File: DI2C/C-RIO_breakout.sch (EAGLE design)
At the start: 36 parts, among them X1 GLX-S-88M, X2 GLX-S-88M, X3 GLX-S-88M, X4 GLX-S-88M

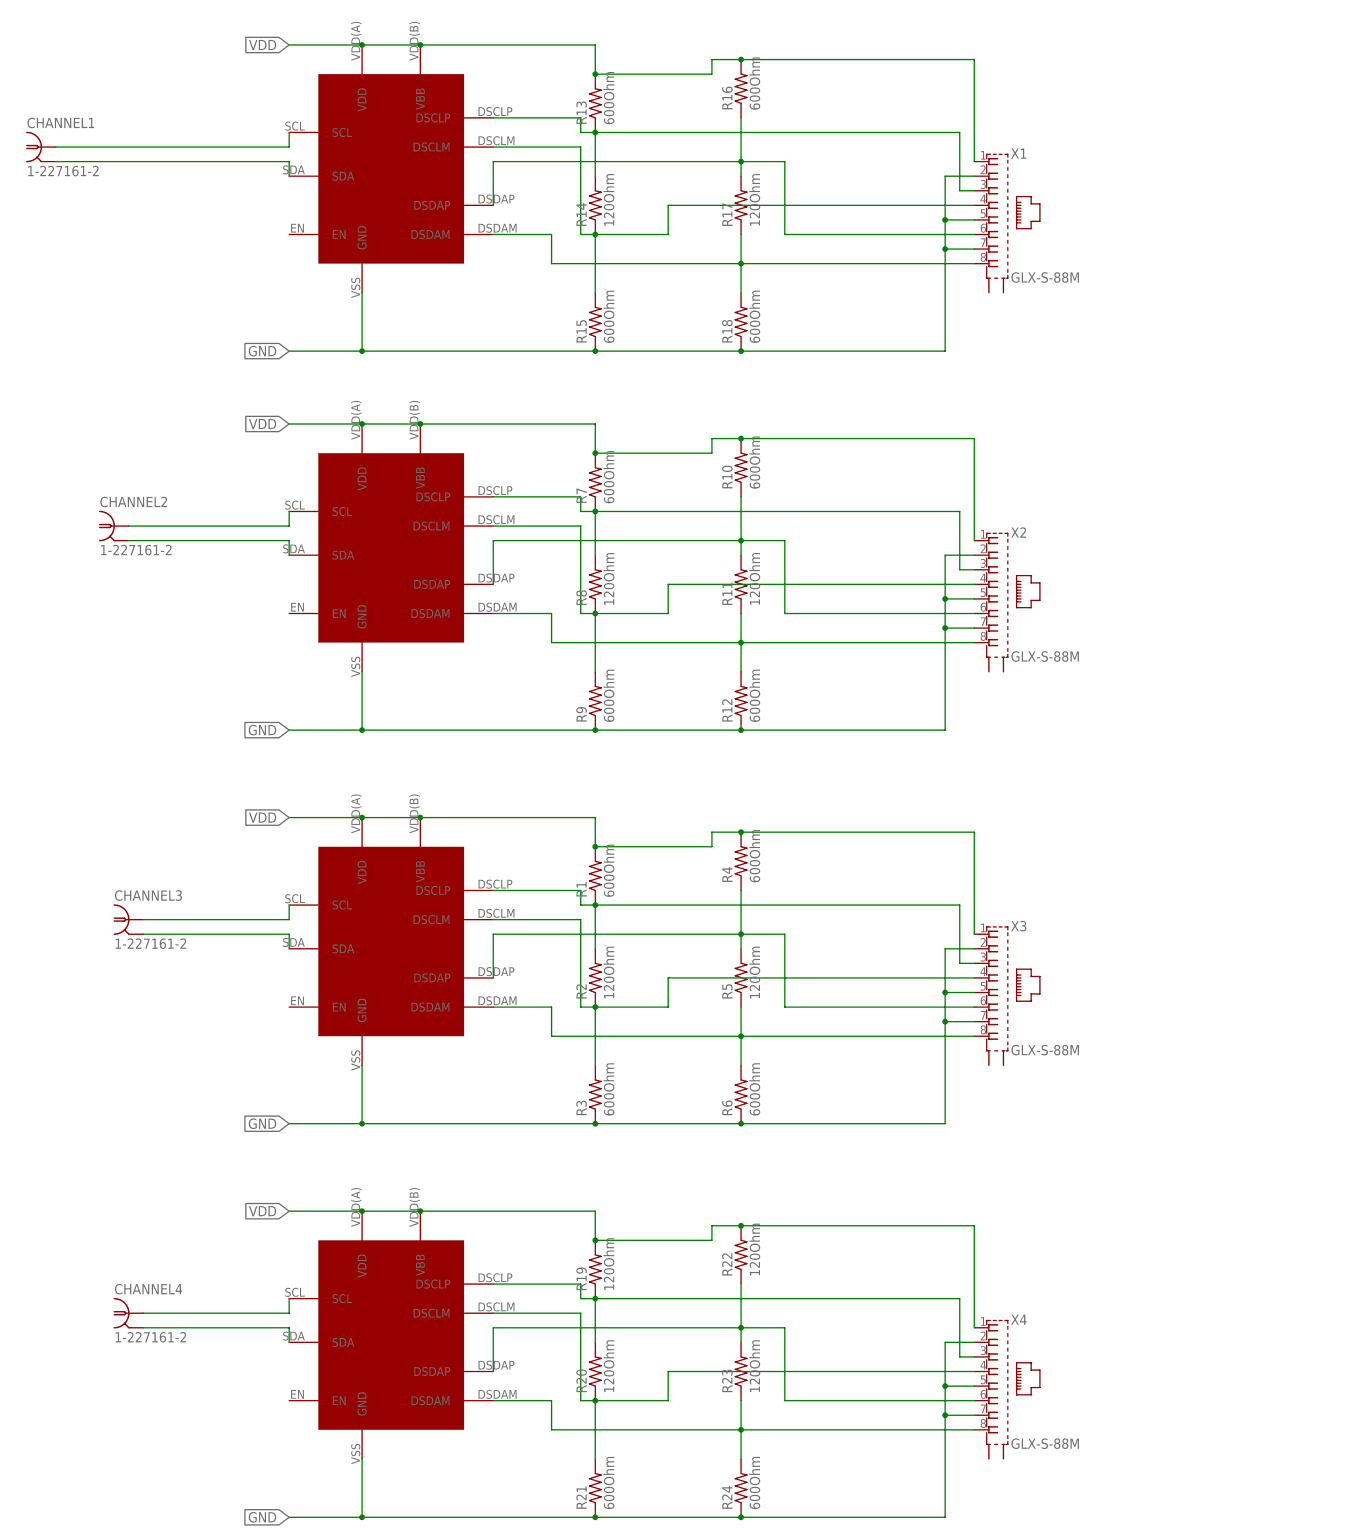
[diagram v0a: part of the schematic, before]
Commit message: finish i2c base master board
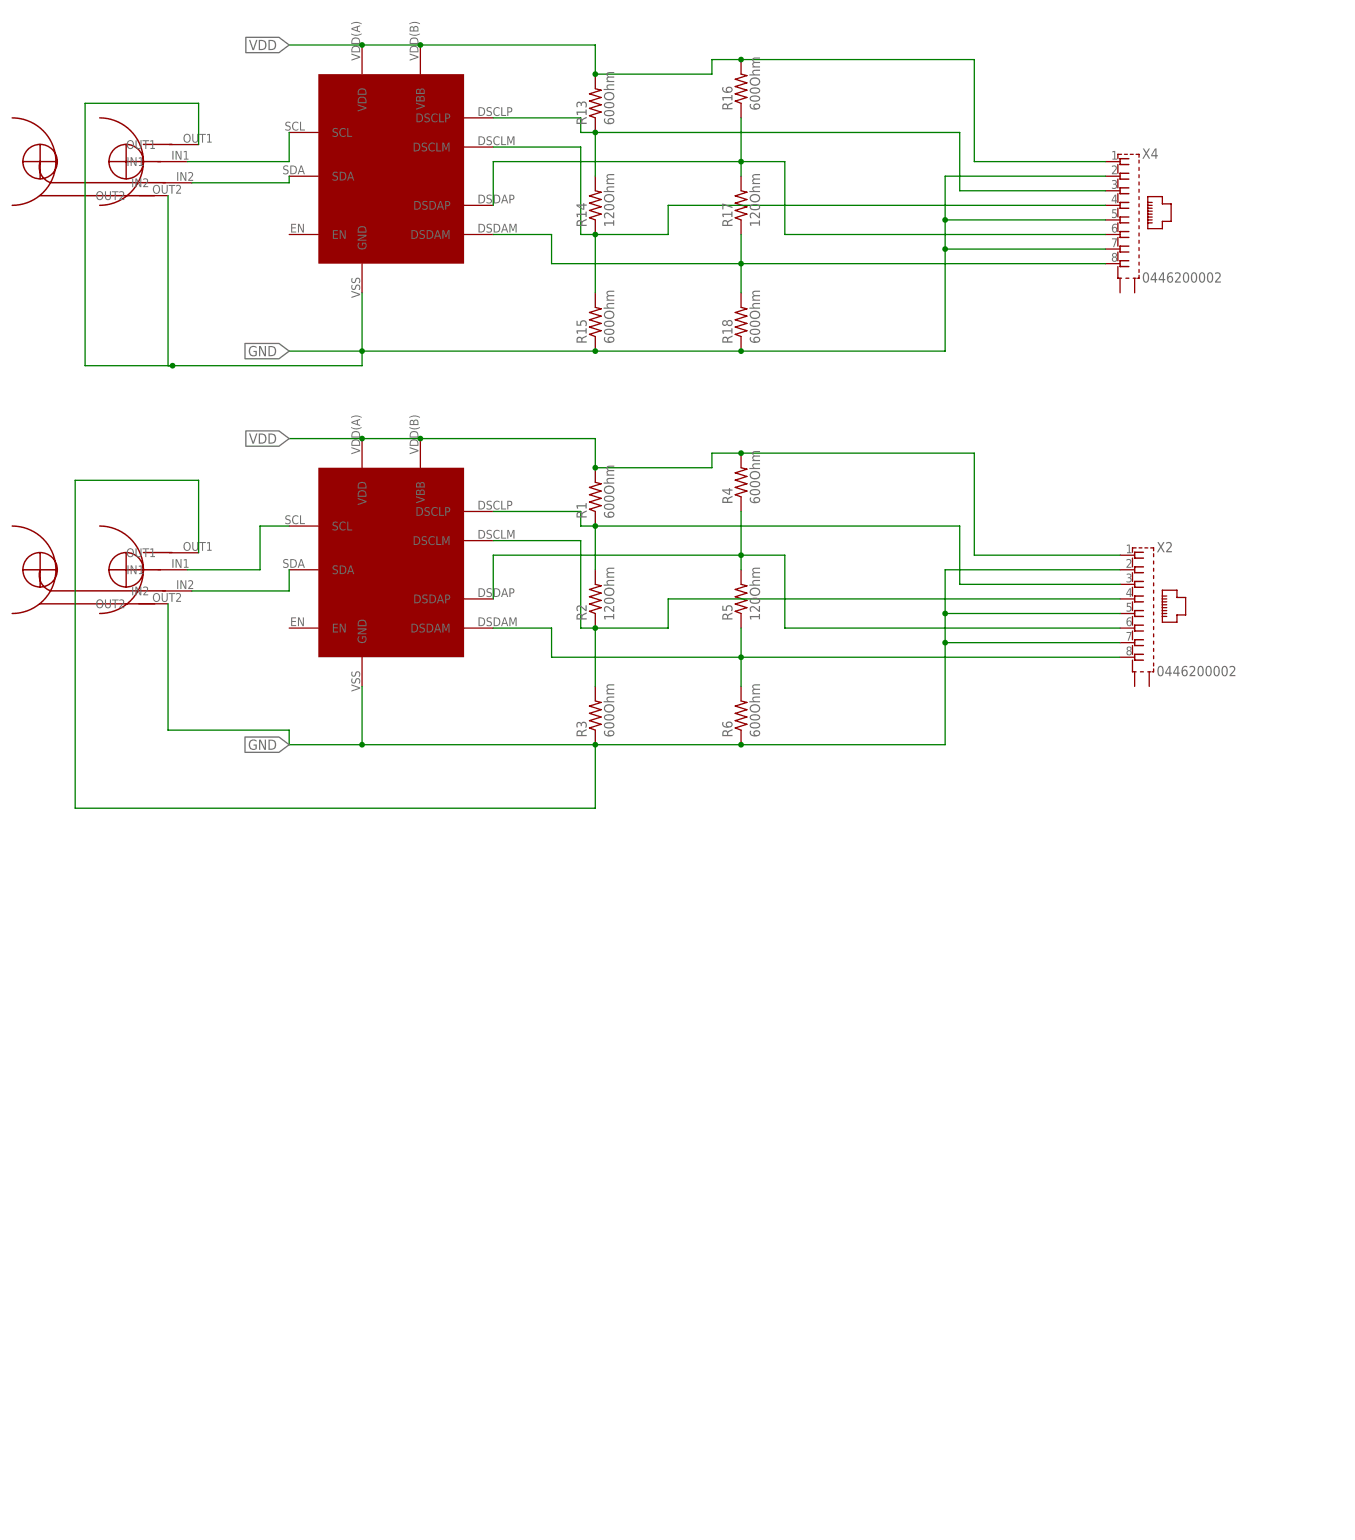
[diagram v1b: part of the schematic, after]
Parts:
- removed CHANNEL1, CHANNEL2, CHANNEL3, CHANNEL4: 1-227161-2, con-coax:1-227161-2
- removed R10, R12, R21, R24, R7, R9: 600Ohm, resistor:R-US_0414/15
- removed R11, R19, R20, R22, R23, R8: 120Ohm, resistor:R-US_0414/15
- removed X1, X3: GLX-S-88M, con-kycon:GLX-S-88M
- U$2, U$4: value PCA9615 -> DUALBNC_CONNECTOR; device PCA9615:PCA9615 -> PCA9615:DUALBNC_CONNECTOR
- X2, X4: value GLX-S-88M -> 0446200002; device con-kycon:GLX-S-88M -> con-molex:0446200002
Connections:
- removed net N$10: R11.1, R12.2, U$2.DSDAM, X2.8
- removed net N$13: R22.1, R23.2, U$4.DSDAP, X4.6
- removed net N$14: R23.1, R24.2, U$4.DSDAM, X4.8
- removed net N$17: CHANNEL4.1, U$4.SCL
- removed net N$18: CHANNEL4.2, U$4.SDA
- removed net N$19: CHANNEL3.2, U$1.SDA
- removed net N$20: CHANNEL3.1, U$1.SCL
- removed net N$21: CHANNEL2.2, U$2.SDA
- removed net N$22: CHANNEL2.1, U$2.SCL
- removed net N$23: CHANNEL1.2, U$3.SDA
- removed net N$24: CHANNEL1.1, U$3.SCL
- removed net N$9: R10.1, R11.2, U$2.DSDAP, X2.6
- net GND: now also U$2.OUT1, U$2.OUT2, U$4.OUT1, U$4.OUT2; no longer R12.1, R21.1, R24.1, R9.1, U$2.GND, U$4.GND, X1.2, X1.5, X1.7, X3.2, X3.5, X3.7
- net N$1: now also X2.3; no longer X3.3
- net N$11: now also X4.3; no longer X1.3
- net N$12: now also X4.4; no longer X1.4
- net N$15: now also X4.6; no longer X1.6
- net N$16: now also X4.8; no longer X1.8
- net N$2: now also U$1.SCL, U$4.IN1; no longer R19.1, R20.2, U$4.DSCLP, X4.3
- net N$3: now also X2.4; no longer X3.4
- net N$4: now also X2.6; no longer X3.6
- net N$5: now also X2.8; no longer X3.8
- net N$6: now also U$1.SDA, U$4.IN2; no longer R7.1, R8.2, U$2.DSCLP, X2.3
- net N$7: now also U$2.IN1, U$3.SCL; no longer R20.1, R21.2, U$4.DSCLM, X4.4
- net N$8: now also U$2.IN2, U$3.SDA; no longer R8.1, R9.2, U$2.DSCLM, X2.4
- net VDD: no longer R10.2, R19.2, R22.2, R7.2, U$2.VBB, U$2.VDD, U$4.VBB, U$4.VDD, X1.1, X3.1
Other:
- moved on the sheet: R1, R2, R3, R4, R5, R6

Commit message: update schmeatic
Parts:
- removed X2, X4: 0446200002, con-molex:0446200002
- added R10, R7, R8, R9: 600Ohm, resistor:R-US_0414/15
- added T1, T2, T3, T4: 2N2222, transistor-neu-to92:2N2222
- added TOF1, TOF2, TOF3, TOF4, U$6: RJ45-8N4-B, con-amphenol-rj45-ld:RJ45-8N4-B
- added X1: (no value), con-subd:F37HPS
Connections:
- net N$2 renamed SCL1
- net N$6 renamed SDA1
- net N$7 renamed SCL2
- net N$8 renamed SDA2
- removed net N$1: R1.1, R2.2, U$1.DSCLP, X2.3
- removed net N$3: R2.1, R3.2, U$1.DSCLM, X2.4
- removed net N$5: R5.1, R6.2, U$1.DSDAM, X2.8
- new net DSCLM1: R2.1, R3.2, TOF1.NC1, TOF2.NC1, TOF3.NC1, TOF4.NC1, U$1.DSCLM
- new net DSCLP1: R1.1, R2.2, TOF1.TX-, TOF2.TX-, TOF3.TX-, TOF4.TX-, U$1.DSCLP
- new net DSDAM1: R5.1, R6.2, TOF1.TX0, TOF2.TX0, TOF3.TX0, TOF4.TX0, U$1.DSDAM
- new net DSDAP1: TOF1.RX0, TOF2.RX0, TOF3.RX0, TOF4.RX0
- new net GND2: TOF1.GND1, TOF1.GND2, TOF2.GND1, TOF2.GND2, TOF3.GND1, TOF3.GND2, TOF4.GND1, TOF4.GND2
- net GND: now also T1.C, T1.E, T2.C, T2.E, T3.C, T3.E, T4.C, T4.E, TOF1.GND, TOF1.RX+, TOF1.RX-, TOF2.GND, TOF2.RX+, TOF2.RX-, TOF3.GND, TOF3.RX+, TOF3.RX-, TOF4.GND, TOF4.RX+, TOF4.RX-, U$6.GND, U$6.GND1, U$6.GND2, U$6.RX0, U$6.TX0; no longer X2.2, X2.5, X2.7, X4.2, X4.5, X4.7
- net N$11: now also U$6.TX-; no longer X4.3
- net N$12: now also U$6.RX+; no longer X4.4
- net N$15: now also U$6.RX-; no longer X4.6
- net N$16: now also U$6.NC1; no longer X4.8
- net N$4: no longer X2.6
- net VDD: now also R10.1, R10.2, R7.1, R7.2, R8.1, R8.2, R9.1, R9.2, TOF1.TX+, TOF2.TX+, TOF3.TX+, TOF4.TX+, U$6.TX+; no longer X2.1, X4.1

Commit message: added the lsave board
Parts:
- added COMMON: RJ45-8N4-B, con-amphenol-rj45-ld:RJ45-8N4-B
- added SV1: (no value), con-lstb:MA06-1
- added X2, X3: (no value), con-wago-508:W237-08P
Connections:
- new net AI0: X1-7.F, X2-1.KL
- new net AI1: X1-8.F, X2-2.KL
- new net AI2: X1-9.F, X2-3.KL
- new net AI3: X1-10.F, X2-4.KL
- new net AI4: X1-11.F, X2-5.KL
- new net AI5: X1-12.F, X2-6.KL
- new net AI6: X1-13.F, X2-7.KL
- new net AI7: X1-14.F, X2-8.KL
- new net AO0: X1-1.F, X3-1.KL
- new net AO1: X1-2.F, X3-2.KL
- new net AO2: X1-21.F, X3-3.KL
- new net AO3: X1-22.F, X3-4.KL
- new net AO4: X1-4.F, X3-5.KL
- new net AO5: X1-5.F, X3-6.KL
- new net AO6: X1-24.F, X3-7.KL
- new net AO7: X1-25.F, X3-8.KL
- new net DIO0: T3.B, X1-15.F
- new net DIO1: T4.B, X1-16.F
- new net DIO2: T2.B, X1-17.F
- new net DIO3: T1.B, X1-18.F
- new net GNDT1: T1.C, TOF4.GND
- new net GNDT2: T2.C, TOF3.GND
- new net GNDT3: T3.C, TOF1.GND
- new net GNDT4: T4.C, TOF2.GND
- net DSCLM1: now also COMMON.NC1
- net DSCLP1: now also COMMON.TX-
- net DSDAM1: now also COMMON.TX0
- net DSDAP1: now also COMMON.RX0
- net GND: now also COMMON.GND, COMMON.GND1, COMMON.GND2, COMMON.RX+, COMMON.RX-, SV1.2, X1-19.F, X1-20.F, X1-23.F, X1-26.F, X1-27.F, X1-28.F, X1-29.F, X1-3.F, X1-30.F, X1-31.F, X1-32.F, X1-33.F, X1-34.F, X1-35.F, X1-36.F, X1-37.F, X1-6.F; no longer T1.C, T2.C, T3.C, T4.C, TOF1.GND, TOF2.GND, TOF3.GND, TOF4.GND
- net SCL1: now also SV1.3
- net SDA1: now also SV1.4
- net VDD: now also COMMON.TX+, SV1.1
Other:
- moved on the sheet: X1-1, X1-10, X1-11, X1-12, X1-13, X1-14, X1-15, X1-16, X1-17, X1-18, X1-19, X1-2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
